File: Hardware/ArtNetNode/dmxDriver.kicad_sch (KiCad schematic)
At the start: 17 parts, among them IC2 ISO1641BDR, J2 B3B-XH-A, U2 MAX485E

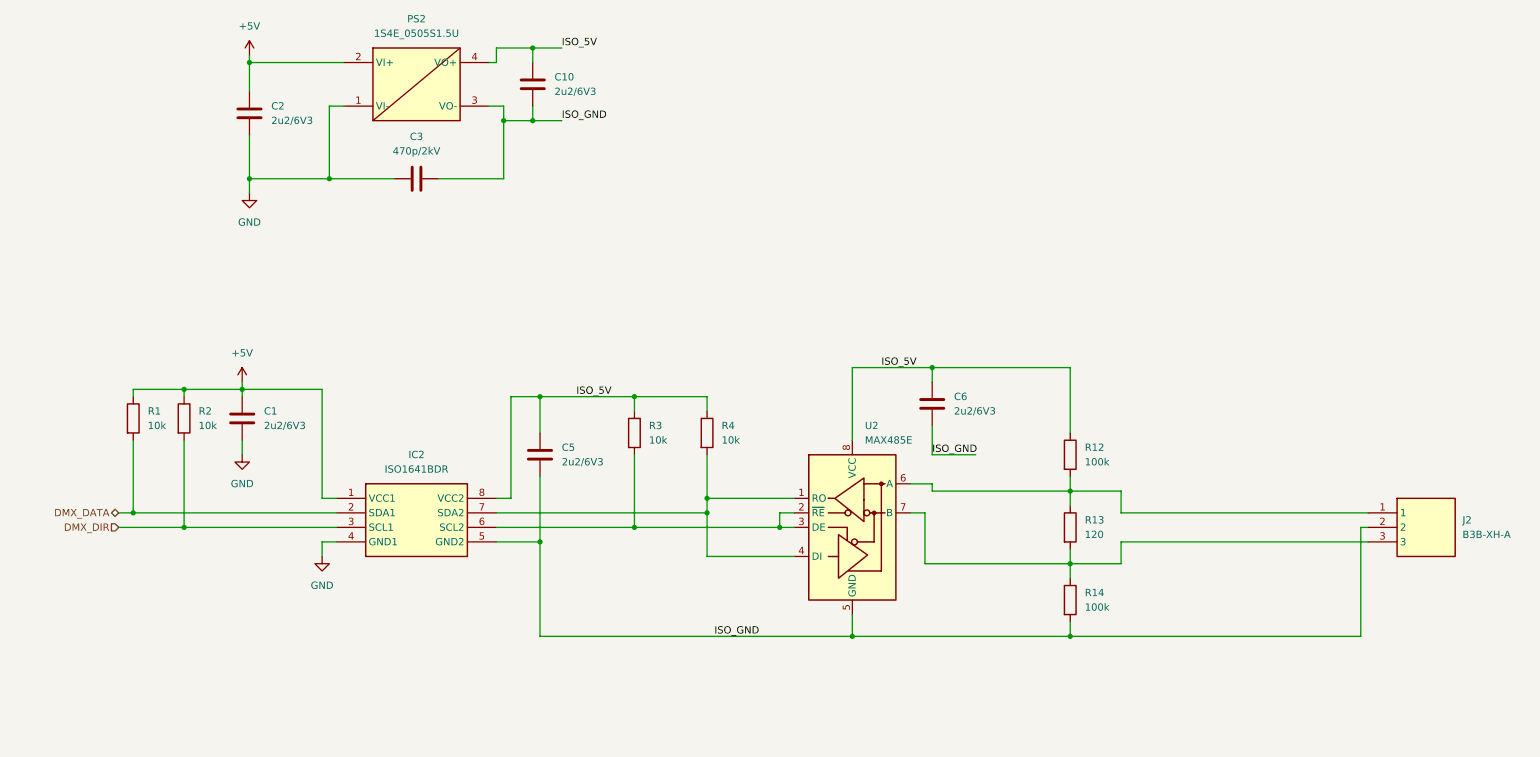
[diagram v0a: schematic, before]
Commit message: added ethernet
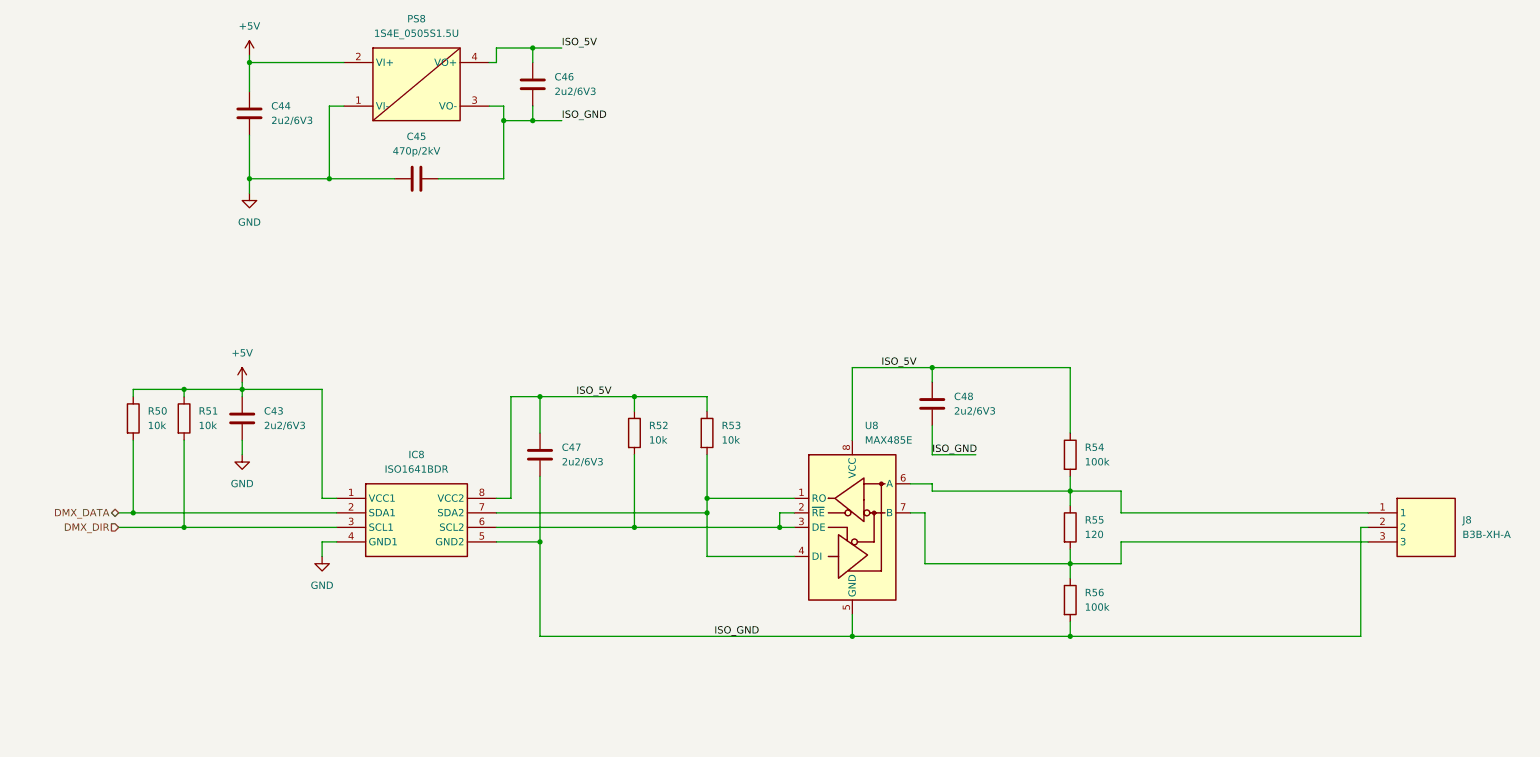
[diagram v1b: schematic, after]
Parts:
- renumbered C1 to C43, C2 to C44, C3 to C45, C10 to C46, C5 to C47, C6 to C48, IC2 to IC8, J2 to J8, PS2 to PS8, R1 to R50, R2 to R51, R3 to R52, R4 to R53, R12 to R54, R13 to R55, R14 to R56, U2 to U8
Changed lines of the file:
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@@
 		(dnp no)
 		(fields_autoplaced yes)
-		(property "Reference" "#PWR08"
+		(property "Reference" "#PWR038"
 			(at 162.56 81.28 0)
 			(effects
@@
 		(dnp no)
 		(fields_autoplaced yes)
-		(property "Reference" "R2"
+		(property "Reference" "R51"
 			(at 153.67 139.6999 0)
 			(effects
@@
 		(dnp no)
 		(fields_autoplaced yes)
-		(property "Reference" "IC2"
+		(property "Reference" "IC8"
 			(at 191.77 147.32 0)
 			(effects
@@
 		(on_board yes)
 		(dnp no)
-		(property "Reference" "C3"
+		(property "Reference" "C45"
 			(at 191.77 91.694 90)
 			(effects
@@
 		(dnp no)
 		(fields_autoplaced yes)
-		(property "Reference" "R13"
+		(property "Reference" "R55"
 			(at 308.61 158.7499 0)
 			(effects
@@
 		(dnp no)
 		(fields_autoplaced yes)
-		(property "Reference" "C5"
+		(property "Reference" "C47"
 			(at 217.17 146.0499 0)
 			(effects
@@
 		(dnp no)
 		(fields_autoplaced yes)
-		(property "Reference" "#PWR01"
+		(property "Reference" "#PWR036"
 			(at 161.29 138.43 0)
 			(effects
@@
 		(dnp no)
 		(fields_autoplaced yes)
-		(property "Reference" "U2"
+		(property "Reference" "U8"
 			(at 270.1641 142.24 0)
 			(effects
@@
 		(dnp no)
 		(fields_autoplaced yes)
-		(property "Reference" "#PWR09"
+		(property "Reference" "#PWR039"
 			(at 162.56 107.95 0)
 			(effects
@@
 		(dnp no)
 		(fields_autoplaced yes)
-		(property "Reference" "#PWR05"
+		(property "Reference" "#PWR040"
 			(at 175.26 171.45 0)
 			(effects
@@
 		(dnp no)
 		(fields_autoplaced yes)
-		(property "Reference" "R12"
+		(property "Reference" "R54"
 			(at 308.61 146.0499 0)
 			(effects
@@
 		(dnp no)
 		(fields_autoplaced yes)
-		(property "Reference" "C10"
+		(property "Reference" "C46"
 			(at 215.9 81.2799 0)
 			(effects
@@
 		(dnp no)
 		(fields_autoplaced yes)
-		(property "Reference" "R14"
+		(property "Reference" "R56"
 			(at 308.61 171.4499 0)
 			(effects
@@
 		(dnp no)
 		(fields_autoplaced yes)
-		(property "Reference" "PS2"
+		(property "Reference" "PS8"
 			(at 191.77 71.12 0)
 			(effects
@@
 		(dnp no)
 		(fields_autoplaced yes)
-		(property "Reference" "C6"
+		(property "Reference" "C48"
 			(at 285.75 137.1599 0)
 			(effects
@@
 		(dnp no)
 		(fields_autoplaced yes)
-		(property "Reference" "C2"
+		(property "Reference" "C44"
 			(at 166.37 86.3599 0)
 			(effects
@@
 		(dnp no)
 		(fields_autoplaced yes)
-		(property "Reference" "J2"
+		(property "Reference" "J8"
 			(at 374.65 158.7499 0)
 			(effects
@@
 		(dnp no)
 		(fields_autoplaced yes)
-		(property "Reference" "R1"
+		(property "Reference" "R50"
 			(at 144.78 139.6999 0)
 			(effects
@@
 		(dnp no)
 		(fields_autoplaced yes)
-		(property "Reference" "#PWR02"
+		(property "Reference" "#PWR037"
 			(at 161.29 153.67 0)
 			(effects
@@
 		(dnp no)
 		(fields_autoplaced yes)
-		(property "Reference" "C1"
+		(property "Reference" "C43"
 			(at 165.1 139.6999 0)
 			(effects
@@
 		(dnp no)
 		(fields_autoplaced yes)
-		(property "Reference" "R3"
+		(property "Reference" "R52"
 			(at 232.41 142.2399 0)
 			(effects
@@
 		(dnp no)
 		(fields_autoplaced yes)
-		(property "Reference" "R4"
+		(property "Reference" "R53"
 			(at 245.11 142.2399 0)
 			(effects

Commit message: finished dmx interfaces
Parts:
- removed C43, C47: 2u2/6V3, Capacitor_SMD:C_0603_1608Metric, symbol Device:C
- removed IC8: ISO1641BDR, SamacSys_Parts:SOIC127P600X175-8N, symbol SamacSys_Parts:ISO1641BDR
- added R3, R4, R6: 100, Resistor_SMD:R_0603_1608Metric, symbol Device:R
- added R5, R7, R71: 10k, Resistor_SMD:R_0603_1608Metric, symbol Device:R
- added R63, R67: 0, Resistor_SMD:R_0603_1608Metric, symbol Device:R
- added U6, U7, U8: LTV-356T, Package_SO:SO-4_4.4x3.6mm_P2.54mm, symbol Isolator:LTV-356T
- renumbered C44 to C1, C45 to C2, C46 to C3, C48 to C4, J8 to J1, PS8 to PS1, R50 to R1, R54 to R10, R55 to R11, R56 to R12, R51 to R2, R52 to R8, R53 to R9, U8 to U4
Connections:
- net +5V: no longer R1.1, R2.1
- net GND: now also R5.2
- net ISO_5V: now also R7.1
- net ISO_GND: now also R67.2, U6.2, U7.3, U8.3
- net at R8.2, U4.3 (DE): now also R63.2, U7.4; no longer U4.2 (~{RE})
- net at R9.2, U4.1 (RO): now also R6.2; no longer U4.4 (DI)
- net DMX_DATA renamed TX
- net TX: now also U8.2
- net DMX_DIR renamed DIR
- net DIR: now also U7.2
- new net: R7.2, U4.4 (DI), U8.4
- new net: R63.1, R67.1, U4.2 (~{RE})
- new net: R3.1, U8.1
- new net: R4.1, U7.1
- new net: R6.1, U6.1
- new net +3.3V: R1.1, R2.1, R3.2, R4.2, R71.1, U6.4
- new net RX: R5.1, R71.2, U6.3
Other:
- moved on the sheet: R1, R2, R8, R9
